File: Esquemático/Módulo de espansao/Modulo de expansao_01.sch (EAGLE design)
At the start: 92 parts, among them IC1 MCP25050-I/P, IC2 MCP2551-I/P, IC3 LM1117T-3.3/NOPB, K1 AQV21, K2 AQV21, K3 AQV21, K4 AQV21, K5 AQV21, K6 AQV21, Q2 20M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

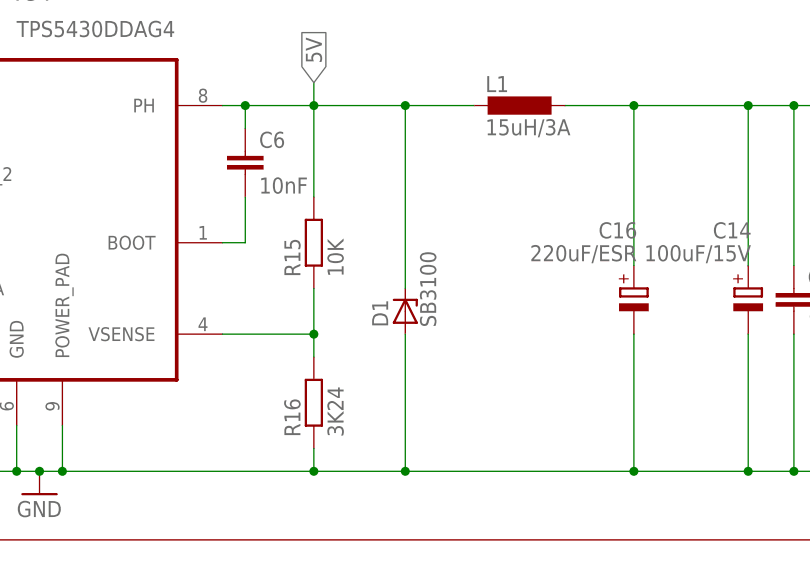
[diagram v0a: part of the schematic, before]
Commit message: modulo de expansao final
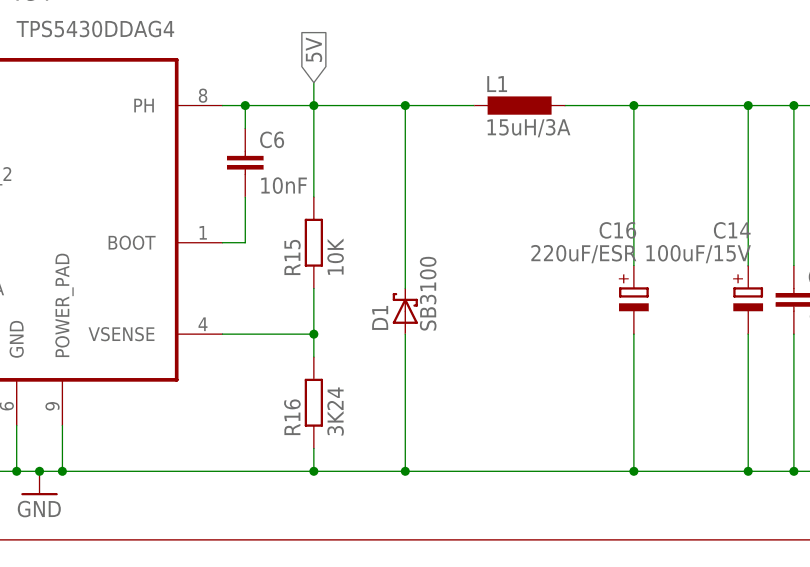
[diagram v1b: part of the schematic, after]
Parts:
- D1: device diode:BZV10 -> diode:SCHOTTKY-DIODEDO201T15
- D2: device diode:AA112 -> diode:1N5624
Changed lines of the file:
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@@
 <part name="C14" library="rcl" deviceset="CPOL-EU" device="E2-5" value="100uF/15V"/>
 <part name="C15" library="rcl" deviceset="CPOL-EU" device="E2-5" value="10uF/15V"/>
-<part name="D2" library="diode" deviceset="AA112" device="" value="1N5400G-T"/>
+<part name="D2" library="diode" deviceset="1N5624" device="" value="1N5400G-T"/>
 <part name="D9" library="diode" deviceset="BZV10" device="" value="BZV85C33"/>
 <part name="C16" library="rcl" deviceset="CPOL-EU" device="E2.5-7" value="220uF/ESR"/>
@@
 <part name="R15" library="rcl" deviceset="R-EU_" device="0207/10" value="10K"/>
 <part name="R16" library="rcl" deviceset="R-EU_" device="0207/10" value="3K24"/>
-<part name="D1" library="diode" deviceset="BZV10" device="" value="SB3100"/>
+<part name="D1" library="diode" deviceset="SCHOTTKY-DIODE" device="DO201T15" value="SB3100"/>
 <part name="C6" library="rcl" deviceset="C-EU" device="025-025X050" value="10nF"/>
 <part name="R4" library="rcl" deviceset="R-EU_" device="0207/10" value="1K"/>
@@
 <instance part="R15" gate="G$1" x="-119.38" y="314.96" rot="R90"/>
 <instance part="R16" gate="G$1" x="-119.38" y="297.18" rot="R90"/>
-<instance part="D1" gate="1" x="-109.22" y="307.34" rot="R90"/>
+<instance part="D1" gate="G$1" x="-109.22" y="307.34" smashed="yes" rot="R90">
+<attribute name="NAME" x="-111.125" y="305.054" size="1.778" layer="95" rot="R90"/>
+<attribute name="VALUE" x="-105.791" y="305.054" size="1.778" layer="96" rot="R90"/>
+</instance>
 <instance part="C6" gate="G$1" x="-127" y="325.12"/>
 <instance part="R4" gate="G$1" x="-132.08" y="137.16"/>
@@
 <junction x="-109.22" y="330.2"/>
 <pinref part="L1" gate="G$1" pin="2"/>
-<pinref part="D1" gate="1" pin="C"/>
+<pinref part="D1" gate="G$1" pin="C"/>
 <pinref part="C6" gate="G$1" pin="1"/>
 <pinref part="R15" gate="G$1" pin="2"/>
@@
 <pinref part="C3" gate="G$1" pin="2"/>
 <pinref part="C4" gate="G$1" pin="2"/>
-<pinref part="D1" gate="1" pin="A"/>
+<pinref part="D1" gate="G$1" pin="A"/>
 <wire x1="-147.32" y1="289.56" x2="-119.38" y2="289.56" width="0.1524" layer="91"/>
 <pinref part="R16" gate="G$1" pin="1"/>
